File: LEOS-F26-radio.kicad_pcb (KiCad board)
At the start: 2 copper layers, 100 x 100 mm, 18 parts, among them J1 MicroFit_1x4, J2 MicroFit_1x4, U1 MCP2518FD, U2 MCP2562FD, Y1 40 MHz

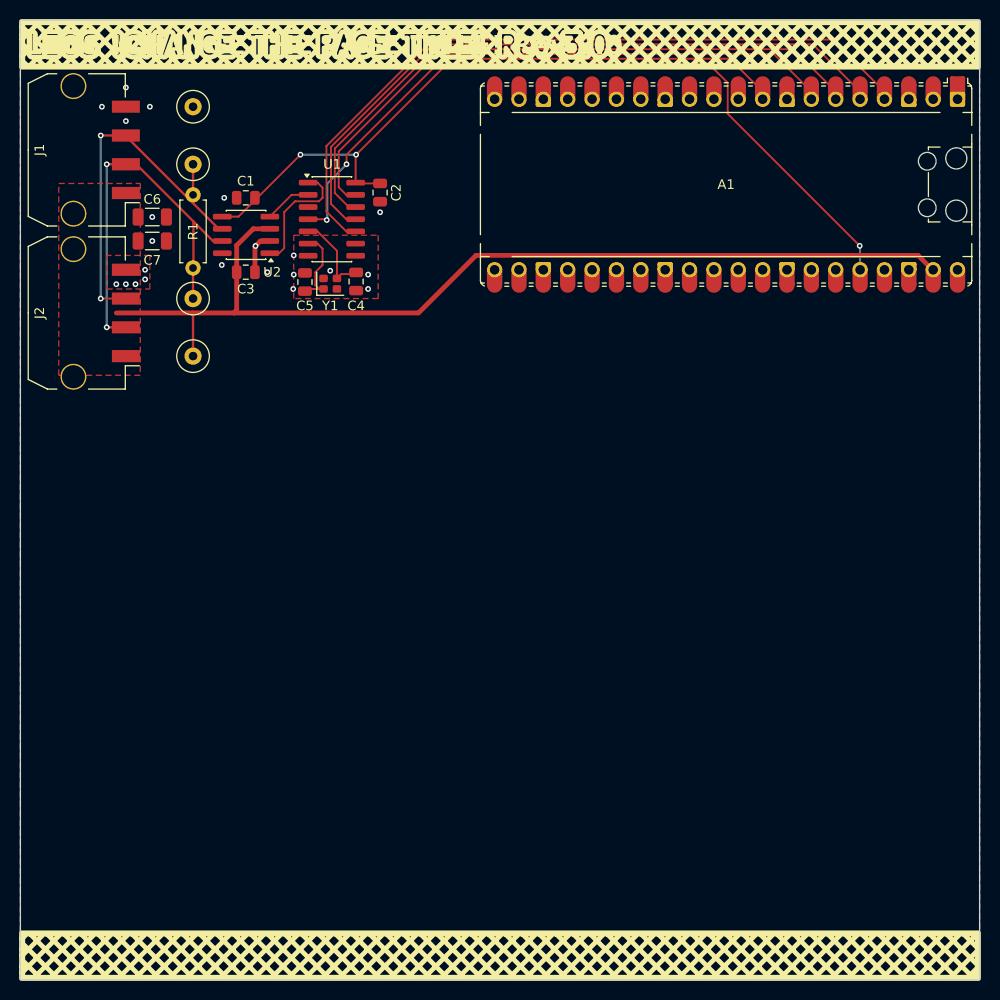
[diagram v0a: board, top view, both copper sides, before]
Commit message: schematic and routing updated
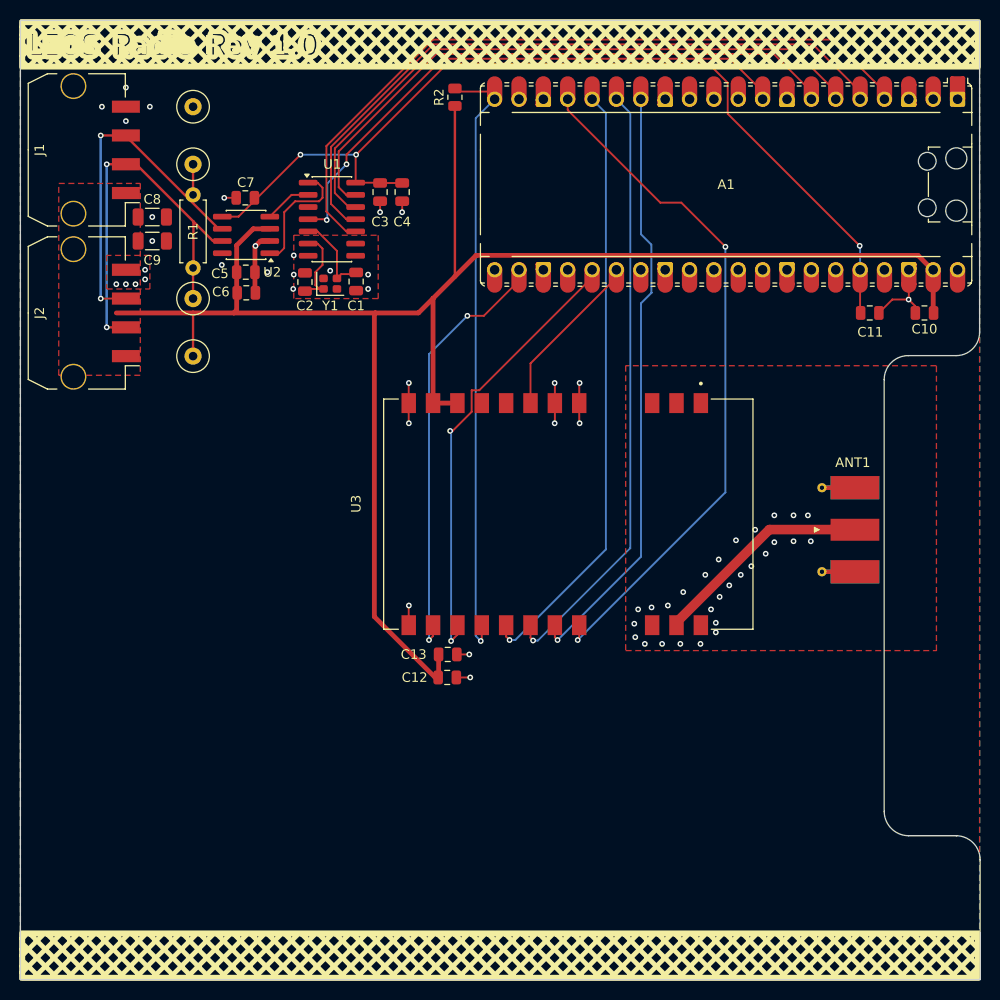
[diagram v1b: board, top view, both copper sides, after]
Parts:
- added ANT1: 900MHz SMA, Connector_Coaxial:SMA_Molex_73251-1153_EdgeMount_Horizontal, F.Cu at (185.3, 103.1)
- added C10: 0.1u, Capacitor_SMD:C_0805_2012Metric, F.Cu at (194.2, 80.5)
- added C11: 10u, Capacitor_SMD:C_0805_2012Metric, F.Cu at (188.6, 80.5)
- added C12: 0.1u, Capacitor_SMD:C_0805_2012Metric, F.Cu at (144.5, 118.5)
- added C13: 1u, Capacitor_SMD:C_0805_2012Metric, F.Cu at (144.6, 116.1)
- added C4: 1u, Capacitor_SMD:C_0805_2012Metric, F.Cu at (139.8, 67.9)
- added C6: 1u, Capacitor_SMD:C_0805_2012Metric, F.Cu at (123.5, 78.4)
- added R2: 10k, Resistor_SMD:R_0805_2012Metric, F.Cu at (145.3, 58.0)
- added U3: E22-900M30S, LEOS:XCVR_E22-900M30S, F.Cu at (157.1, 101.5)
- moved C7 14.1 mm to (123.5, 68.5), turned to 180 degrees
- moved C3 14.0 mm to (137.5, 67.9), turned to -90 degrees
- renumbered C4 to C1, C5 to C2, C1 to C3, C3 to C5, C2 to C7, C6 to C8, C7 to C9
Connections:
- A1 pad 14: unconnected-(A1-GPIO10-Pad14) -> /RF/SCK
- A1 pad 15: unconnected-(A1-GPIO11-Pad15)_1 -> /RF/MOSI
- A1 pad 16: unconnected-(A1-GPIO12-Pad16) -> /RF/MISO
- A1 pad 17: unconnected-(A1-GPIO13-Pad17) -> /RF/CS
- A1 pad 20: unconnected-(A1-GPIO15-Pad20) -> /RF/nRESET
- A1 pad 22: unconnected-(A1-GPIO17-Pad22)_1 -> /RF/INT
- A1 pad 25: unconnected-(A1-GPIO19-Pad25) -> /RF/BUSY
- A1 pad 26: unconnected-(A1-GPIO20-Pad26)_1 -> /RF/RXEN
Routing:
- net +5V: track 104.0 -> 185.0 mm
- net /RF/CS: track 0.00 -> 72.5 mm, vias 0 -> 2
- net /RF/nRESET: track 0.00 -> 63.5 mm, vias 0 -> 1
- net /RF/MOSI: track 0.00 -> 63.2 mm, vias 0 -> 1
- net /RF/MISO: track 0.00 -> 63.2 mm, vias 0 -> 1
- net /RF/SCK: track 0.00 -> 62.6 mm, vias 0 -> 1
- net /RF/BUSY: track 0.00 -> 46.6 mm, vias 0 -> 2
- net /RF/INT: track 0.00 -> 45.2 mm, vias 0 -> 2
- net GND: track 4.46 -> 35.3 mm, vias 22 -> 61
- net Net-(ANT1-In): track 0.00 -> 23.1 mm
- net /RF/RXEN: track 0.00 -> 16.8 mm
- net VDD: track 90.8 -> 98.0 mm
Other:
- board size 100 x 100 mm -> 100.1 x 100 mm
- board text removed: "Be sure to update the information block at the bottom of the page! (Then delete me)"

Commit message: added silkscreen
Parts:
- added G***: LOGO, LOGO, F.Cu at (120.9, 116.5)
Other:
- board text added: "I'VE MADE THESE BOARDS BEFORE!"

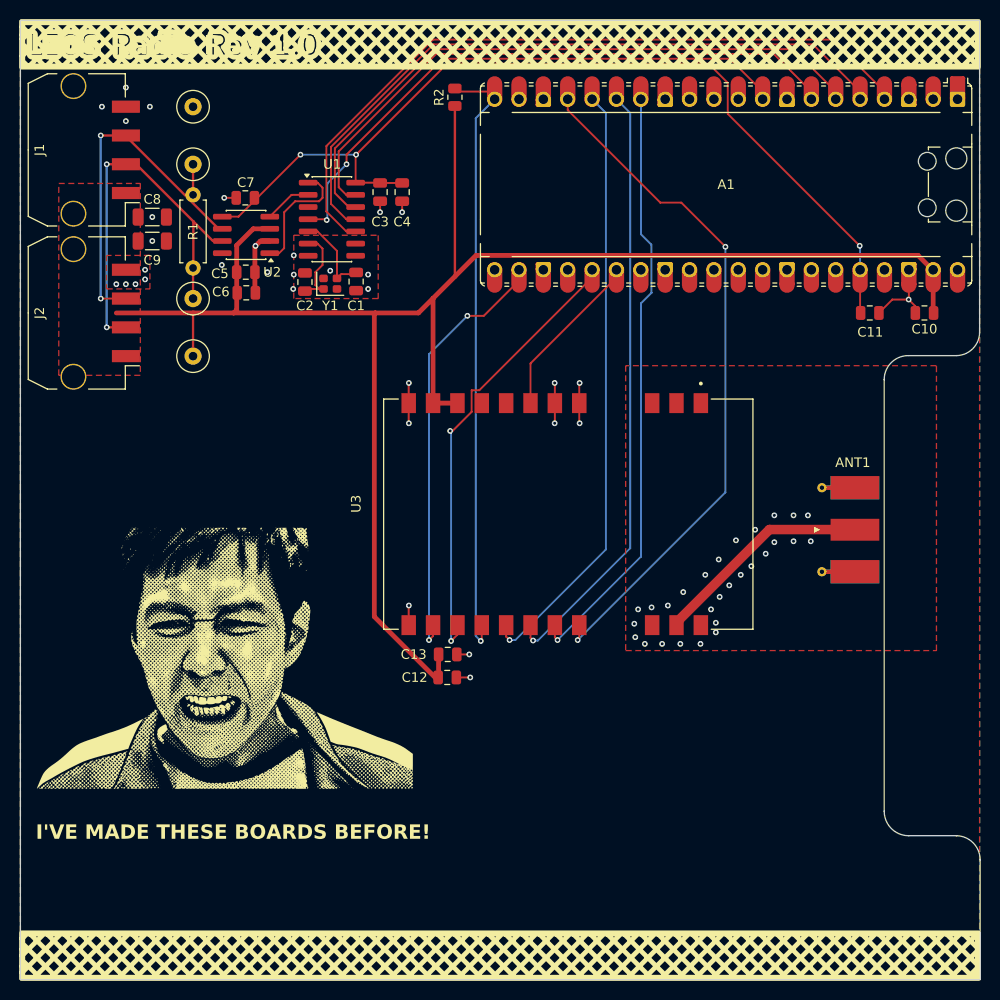
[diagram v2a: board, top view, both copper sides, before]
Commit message: Update routing and edge cuts for RF. Rearrange silkscreen
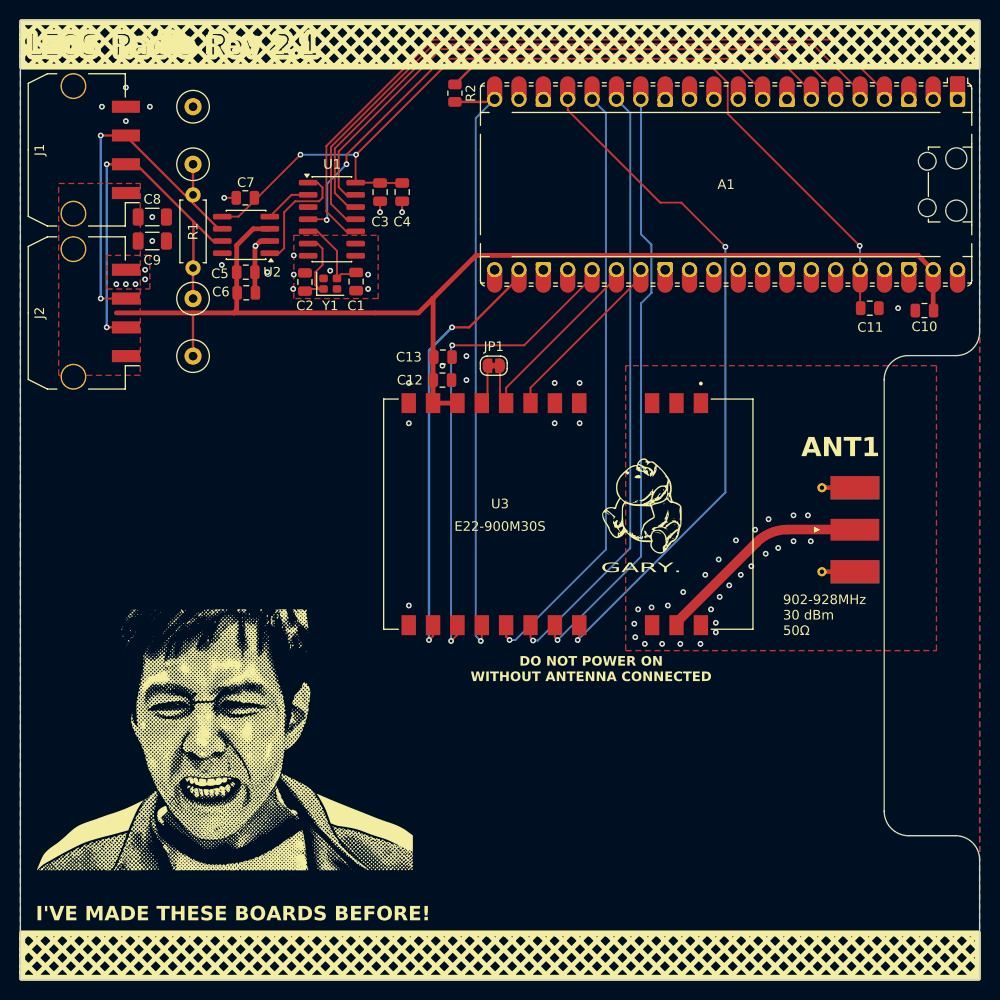
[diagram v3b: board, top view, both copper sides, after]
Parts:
- added JP1: SolderJumper_2_Bridged, Jumper:SolderJumper-2_P1.3mm_Bridged_RoundedPad1.0x1.5mm, F.Cu at (149.3, 86.0)
- moved C12 31.0 mm to (144.0, 87.5)
- moved C13 31.0 mm to (144.1, 85.1)
- moved G*** 8.50 mm to (120.9, 125.0)
- moved C11 0.50 mm to (188.6, 80.0)
- moved R2 0.43 mm to (145.3, 57.6), turned to -90 degrees
- moved C10 0.25 mm to (194.2, 80.2)
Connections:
- net Net-(ANT1-In) renamed /RF/ANT
- A1 pad 26: /RF/RXEN -> /RF/TXEN
- A1 pad 27: unconnected-(A1-GPIO21-Pad27)_1 -> /RF/RXEN
- R2 pad 1: +5V -> VDD
- U3 pad 7: Net-(U3-DIO2) -> /RF/TXEN
- U3 pad 8: Net-(U3-DIO2) -> Net-(JP1-B)
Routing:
- net +5V: track 185.0 -> 123.8 mm
- net GND: track 35.3 -> 10.5 mm, vias 61 -> 62
- net /RF/TXEN: track 0.00 -> 21.1 mm
- net /RF/BUSY: track 46.6 -> 50.3 mm
- net Net-(JP1-B): track 0.00 -> 3.30 mm
- net VDD: track 98.0 -> 100.6 mm
- net /RF/RXEN: track 16.8 -> 17.9 mm
- net /RF/INT: track 45.2 -> 44.5 mm
- net /RF/ANT: track 23.1 -> 22.6 mm
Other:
- board size 100.1 x 100 mm -> 100 x 100 mm
- board text added: "902-928MHz 30 dBm 50Ω"
- board text added: "DO NOT POWER ON WITHOUT ANTENNA CONNECTED"
- board text added: "GARY."
